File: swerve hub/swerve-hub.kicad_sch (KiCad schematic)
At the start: 4 parts

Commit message: canivore hub mostly done
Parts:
- removed J?: RJ12_Shielded, symbol Connector:RJ12_Shielded
- removed SW?: SW_DPST, symbol Switch:SW_DPST
- added J1: RJ45_LED_Shielded, MTJ_88ARX1_FSM_LG:ADAMTECH_MTJ-88ARX1-FSM-LG, symbol Connector:RJ45_LED_Shielded
- added J4: Conn_01x03_Pin, Connector_PinHeader_2.54mm:PinHeader_1x03_P2.54mm_Horizontal, symbol Connector:Conn_01x03_Pin
- added R1: R, Resistor_THT:R_Axial_DIN0207_L6.3mm_D2.5mm_P10.16mm_Horizontal, symbol Device:R
- J2, J3: renamed from J?; footprint (none) -> TerminalBlock_WAGO:TerminalBlock_WAGO_2601-1102_1x02_P3.50mm_Horizontal
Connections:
- net 12v: now also J4.1 (Pin_1)
- net CANh: now also J1.1
- net CANl: now also J1.2
- net GND: now also J1.4, J1.SH, J4.3 (Pin_3), R1.2
- new net: J1.10, J1.3, J4.2 (Pin_2)
- new net: J1.9, R1.1

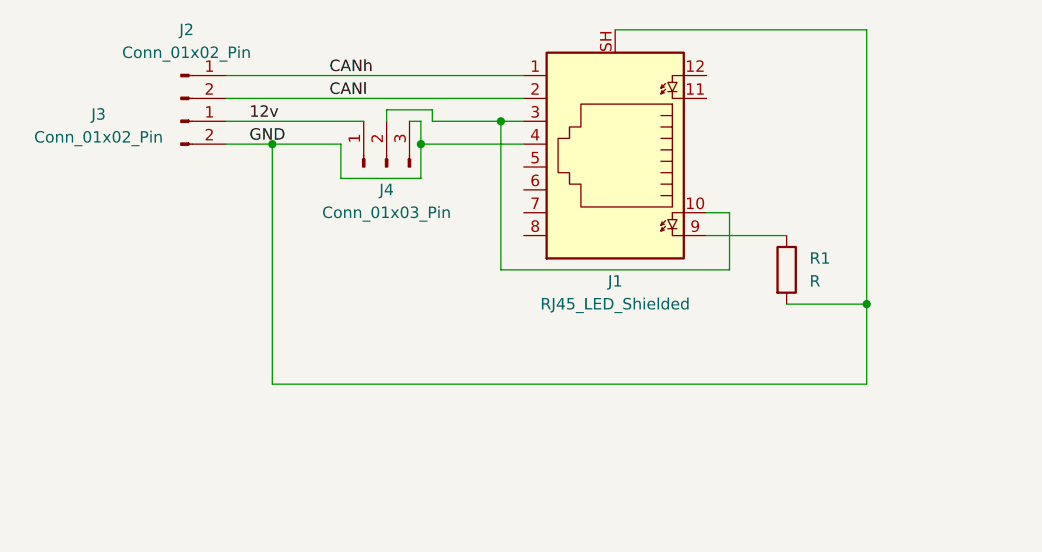
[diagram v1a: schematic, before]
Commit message: swerve hub pcb rearrange and added reverse polarity protection
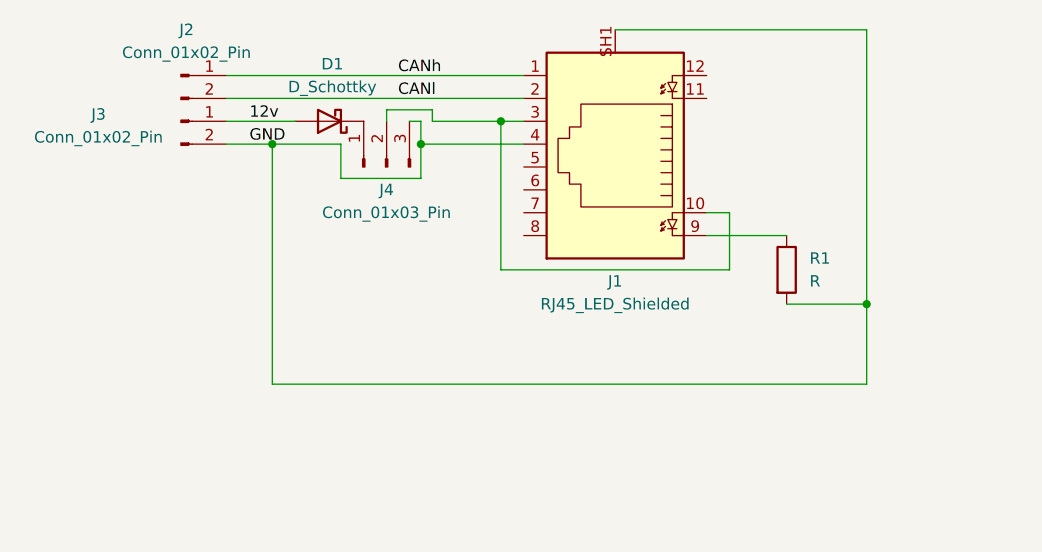
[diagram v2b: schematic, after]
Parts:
- added D1: D_Schottky, Diode_THT:D_DO-41_SOD81_P10.16mm_Horizontal, symbol Device:D_Schottky
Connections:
- net 12v: now also D1.2 (A); no longer J4.1 (Pin_1)
- net GND: now also J1.SH1; no longer J1.SH
- new net: D1.1 (K), J4.1 (Pin_1)
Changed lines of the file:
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@@
 	(wire
 		(pts
-			(xy 118.11 69.85) (xy 133.35 69.85)
+			(xy 118.11 69.85) (xy 125.73 69.85)
 		)
 		(stroke
@@
 	)
 	(label "CANh"
-		(at 129.54 64.77 0)
+		(at 137.16 64.77 0)
 		(effects
 			(font
@@
 	)
 	(label "CANl"
-		(at 129.54 67.31 0)
+		(at 137.16 67.31 0)
 		(effects
 			(font
@@
 		(pin "8"
 		)
-		(pin "SH"
+		(pin "SH1"
 		)
 		(pin "12"
@@
 					(unit 1)
 				)
+			)
+		)
+	)
+	(symbol
+		(lib_id "Device:D_Schottky")
+		(at 129.54 69.85 180)
+		(unit 1)
+		(exclude_from_sim no)
+		(in_bom yes)
+		(on_board yes)
+		(dnp no)
+		(fields_autoplaced yes)
+		(property "Reference" "D1"
+			(at 129.8575 63.5 0)
+			(effects
+				(font
+					(size 1.27 1.27)
+				)
+			)
+		)
+		(property "Value" "D_Schottky"
+			(at 129.8575 66.04 0)
+			(effects
+				(font
+					(size 1.27 1.27)
+				)
+			)
+		)
+		(property "Footprint" "Diode_THT:D_DO-41_SOD81_P10.16mm_Horizontal"
+			(at 129.54 69.85 0)
+			(effects
+				(font
+					(size 1.27 1.27)
+				)
+				(hide yes)
+			)
+		)
+		(property "Datasheet" "~"
+			(at 129.54 69.85 0)
+			(effects
+				(font
+					(size 1.27 1.27)
+				)
+				(hide yes)
+			)
+		)
+		(property "Description" "Schottky diode"
+			(at 129.54 69.85 0)
+			(effects
+				(font
+					(size 1.27 1.27)
+				)
+				(hide yes)
+			)
+		)
+		(pin "2"
+		)
+		(pin "1"
+		)
+		(instances
+			(project ""
+				(path "/1bba0107-a93b-4d94-aa86-4b676137e64e"
+					(reference "D1")
+					(unit 1)
+				)

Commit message: swerve can improvements, ground planes, removed excess wagos
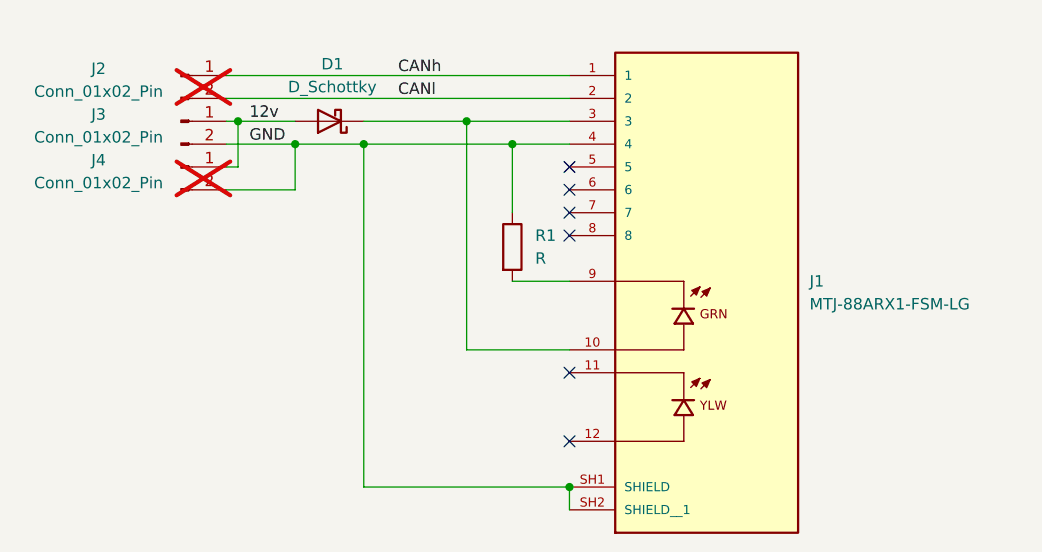
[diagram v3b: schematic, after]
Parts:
- removed J1: RJ45_LED_Shielded, MTJ_88ARX1_FSM_LG:ADAMTECH_MTJ-88ARX1-FSM-LG, symbol Connector:RJ45_LED_Shielded
- removed J4: Conn_01x03_Pin, Connector_PinHeader_2.54mm:PinHeader_1x03_P2.54mm_Horizontal, symbol Connector:Conn_01x03_Pin
- added J1: MTJ-88ARX1-FSM-LG, MTJ_88ARX1_FSM_LG:ADAMTECH_MTJ-88ARX1-FSM-LG, symbol MTJ-88ARX1-FSM-LG:MTJ-88ARX1-FSM-LG
- added J4: Conn_01x02_Pin, Connector_PinHeader_2.54mm:PinHeader_1x02_P2.54mm_Vertical, symbol Connector:Conn_01x02_Pin
- J2: footprint TerminalBlock_WAGO:TerminalBlock_WAGO_2601-1102_1x02_P3.50mm_Horizontal -> Connector_PinHeader_2.54mm:PinHeader_1x02_P2.54mm_Vertical; now not fitted; now left out of the parts list
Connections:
- net 12v: now also J4.1 (Pin_1)
- net CANh: now also J1.1
- net CANl: now also J1.2
- net GND: now also R1.1, J1.4, J1.SH1 (SHIELD), J1.SH2 (SHIELD__1), J4.2 (Pin_2); no longer R1.2
- net at D1.1 (K): now also J1.10, J1.3
- new net: J1.9, R1.2
- no-connect marks 0 -> 6

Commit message: fixed diode placement, major rio hub work
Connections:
- net 12v: now also D1.1 (K), J1.10, J1.3; no longer D1.2 (A), J3.1 (Pin_1)
- new net: D1.2 (A), J3.1 (Pin_1)
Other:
- moved on the sheet: D1
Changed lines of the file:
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@@
-	)
-	(junction
-		(at 119.38 69.85)
-		(diameter 0)
-		(color 0 0 0 0)
 	)
 	(junction
@@
 	)
 	(junction
+		(at 130.81 72.39)
+		(diameter 0)
+		(color 0 0 0 0)
+	)
+	(junction
 		(at 133.35 72.39)
 		(diameter 0)
@@
 	)
 	(junction
-		(at 125.73 72.39)
+		(at 129.54 69.85)
 		(diameter 0)
 		(color 0 0 0 0)
@@
 	(wire
 		(pts
+			(xy 118.11 69.85) (xy 120.65 69.85)
+		)
+		(stroke
+			(width 0)
+			(type default)
+		)
+	)
+	(wire
+		(pts
 			(xy 118.11 64.77) (xy 156.21 64.77)
 		)
@@
 	(wire
 		(pts
-			(xy 125.73 72.39) (xy 133.35 72.39)
-		)
-		(stroke
-			(width 0)
-			(type default)
-		)
-	)
-	(wire
-		(pts
 			(xy 133.35 110.49) (xy 133.35 72.39)
 		)
@@
 	(wire
 		(pts
+			(xy 130.81 72.39) (xy 133.35 72.39)
+		)
+		(stroke
+			(width 0)
+			(type default)
+		)
+	)
+	(wire
+		(pts
 			(xy 133.35 72.39) (xy 149.86 72.39)
 		)
@@
 	(wire
 		(pts
-			(xy 119.38 69.85) (xy 125.73 69.85)
+			(xy 128.27 69.85) (xy 129.54 69.85)
 		)
 		(stroke
@@
 	(wire
 		(pts
-			(xy 118.11 69.85) (xy 119.38 69.85)
-		)
-		(stroke
-			(width 0)
-			(type default)
-		)
-	)
-	(wire
-		(pts
-			(xy 125.73 77.47) (xy 125.73 72.39)
+			(xy 130.81 77.47) (xy 130.81 72.39)
 		)
 		(stroke
@@
 	(wire
 		(pts
-			(xy 118.11 72.39) (xy 125.73 72.39)
+			(xy 118.11 72.39) (xy 130.81 72.39)
 		)
 		(stroke
@@
 	(wire
 		(pts
-			(xy 118.11 77.47) (xy 125.73 77.47)
+			(xy 118.11 77.47) (xy 130.81 77.47)
 		)
 		(stroke
@@
 	(wire
 		(pts
-			(xy 133.35 69.85) (xy 144.78 69.85)
-		)
-		(stroke
-			(width 0)
-			(type default)
-		)
-	)
-	(wire
-		(pts
-			(xy 118.11 74.93) (xy 119.38 74.93)
+			(xy 129.54 69.85) (xy 144.78 69.85)
+		)
+		(stroke
+			(width 0)
+			(type default)
+		)
+	)
+	(wire
+		(pts
+			(xy 118.11 74.93) (xy 129.54 74.93)
 		)
 		(stroke
@@
 	(wire
 		(pts
-			(xy 119.38 74.93) (xy 119.38 69.85)
+			(xy 129.54 74.93) (xy 129.54 69.85)
 		)
 		(stroke
@@
 	)
 	(label "12v"
-		(at 120.65 69.85 0)
+		(at 133.35 69.85 0)
 		(effects
 			(font
@@
 	(symbol
 		(lib_id "Device:D_Schottky")
-		(at 129.54 69.85 180)
+		(at 124.46 69.85 180)
 		(unit 1)
 		(exclude_from_sim no)
@@
 		(fields_autoplaced yes)
 		(property "Reference" "D1"
-			(at 129.8575 63.5 0)
+			(at 124.7775 63.5 0)
 			(effects
 				(font
@@
 		)
 		(property "Value" "D_Schottky"
-			(at 129.8575 66.04 0)
+			(at 124.7775 66.04 0)
 			(effects
 				(font
@@
 		)
 		(property "Footprint" "Diode_THT:D_DO-41_SOD81_P10.16mm_Horizontal"
-			(at 129.54 69.85 0)
+			(at 124.46 69.85 0)
 			(effects
 				(font
@@
 		)
 		(property "Datasheet" "~"
-			(at 129.54 69.85 0)
+			(at 124.46 69.85 0)
 			(effects
 				(font
@@
 		)
 		(property "Description" "Schottky diode"
-			(at 129.54 69.85 0)
+			(at 124.46 69.85 0)
 			(effects
 				(font
@@
 		)
 		(instances
-			(project ""
+			(project "swerve-hub"
 				(path "/1bba0107-a93b-4d94-aa86-4b676137e64e"
 					(reference "D1")
